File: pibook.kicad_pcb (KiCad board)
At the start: 2 copper layers, 85 x 85 mm, 174 parts, among them IC1 ATTINY48-A, J1 ComputeModule, J2 TRS_JACK_3PIN, P1 CONN_01X40, P2 USB_OTG, P3 CONN_01X02, P4 CONN_02X05, P5 USB_A, P6 CONN_02X06, P7 CONN_01X20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

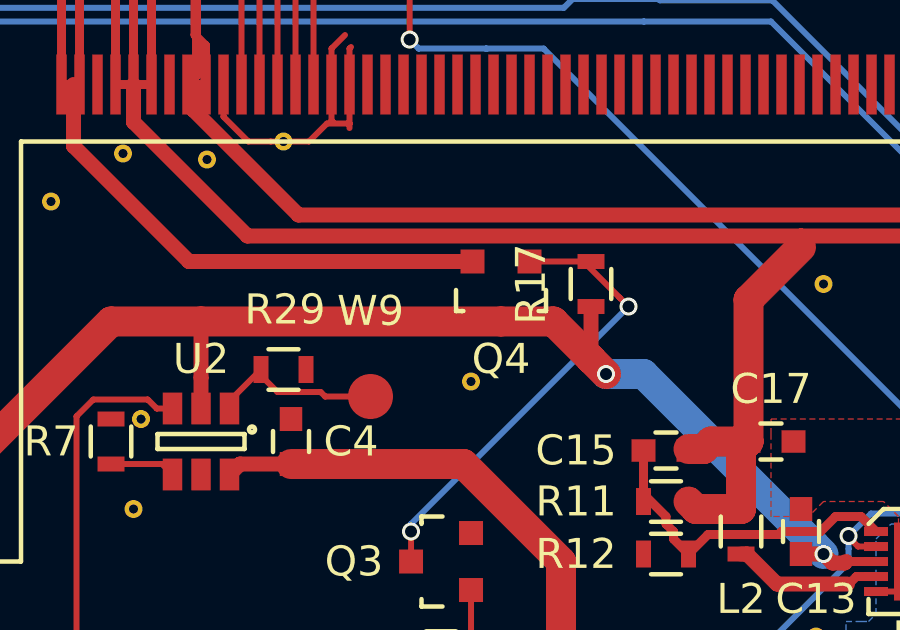
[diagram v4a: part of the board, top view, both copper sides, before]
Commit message: Corrected polarity of mosfet Q4 (switches CM_VBAT)
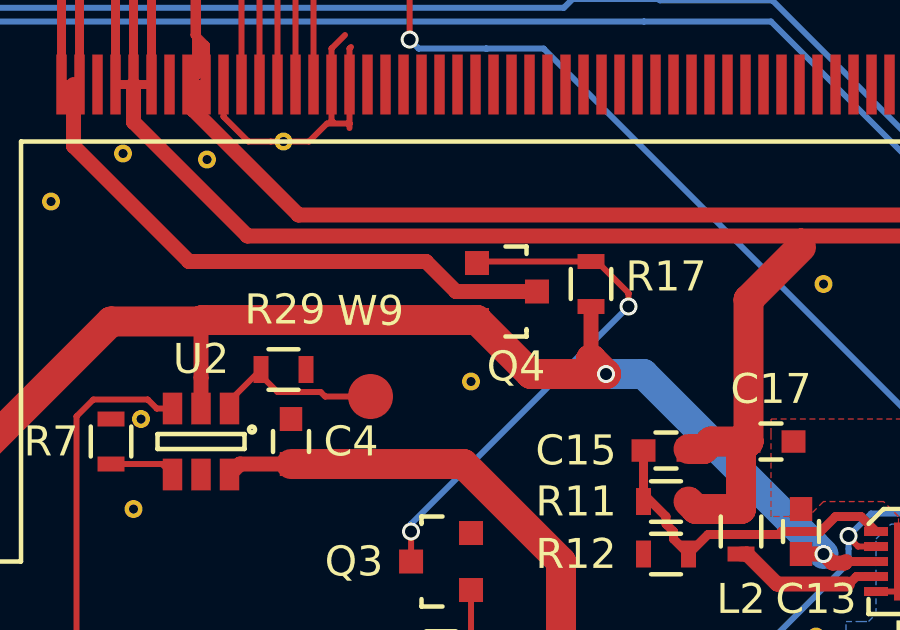
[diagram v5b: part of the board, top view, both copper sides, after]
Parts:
- moved Q4 0.20 mm to (101.2, 176.0), turned to 270 degrees
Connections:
- Q4 pad 2: /CM_VBAT -> +BATT
- Q4 pad 3: +BATT -> /CM_VBAT
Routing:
- net /CM_VBAT: track 38.9 -> 41.5 mm
- net Net-(Q3-Pad3): track 15.4 -> 17.5 mm
- net +BATT: track 300.4 -> 301.2 mm
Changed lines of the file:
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@@
   (general
     (links 404)
-    (no_connects 5)
+    (no_connects 8)
     (area 72.949999 107.949999 158.050001 193.050001)
     (thickness 1.6)
     (drawings 26)
-    (tracks 1700)
+    (tracks 1705)
     (zones 0)
     (modules 174)
@@
   )
   (module TO_SOT_Packages_SMD:SOT-23 (layer F.Cu)
-    (at 101 176 180)
+    (at 101.2 176 270)
     (descr "SOT-23, Standard")
     (tags SOT-23)
     (attr smd)
-    (fp_text reference Q4 (at 0 -2.25 180) (layer F.SilkS)
+    (fp_text reference Q4 (at 2.5 -0.3 360) (layer F.SilkS)
       (effects (font (size 1 1) (thickness 0.15)))
     )
-    (fp_text value Si2323DS (at 0 2.3 180) (layer F.Fab)
+    (fp_text value Si2323DS (at 0 2.3 270) (layer F.Fab)
       (effects (font (size 1 1) (thickness 0.15)))
     )
@@
     (fp_line (start 1.29916 -0.65024) (end 1.49982 -0.65024) (layer F.SilkS) (width 0.15))
     (fp_line (start 1.49982 -0.65024) (end 1.49982 0.0508) (layer F.SilkS) (width 0.15))
-    (pad 1 smd rect (at -0.95 1.00076 180) (size 0.8001 0.8001) (layers F.Cu F.Paste F.Mask)
+    (pad 1 smd rect (at -0.95 1.00076 270) (size 0.8001 0.8001) (layers F.Cu F.Paste F.Mask)
       (net 77 "Net-(Q3-Pad3)"))
-    (pad 2 smd rect (at 0.95 1.00076 180) (size 0.8001 0.8001) (layers F.Cu F.Paste F.Mask)
-      (net 59 /CM_VBAT))
-    (pad 3 smd rect (at 0 -0.99822 180) (size 0.8001 0.8001) (layers F.Cu F.Paste F.Mask)
+    (pad 2 smd rect (at 0.95 1.00076 270) (size 0.8001 0.8001) (layers F.Cu F.Paste F.Mask)
       (net 4 +BATT))
+    (pad 3 smd rect (at 0 -0.99822 270) (size 0.8001 0.8001) (layers F.Cu F.Paste F.Mask)
+      (net 59 /CM_VBAT))
     (model TO_SOT_Packages_SMD.3dshapes/SOT-23.wrl
       (at (xyz 0 0 0))
@@
     (tags "resistor 0603")
     (attr smd)
-    (fp_text reference R17 (at 0 -2 90) (layer F.SilkS)
+    (fp_text reference R17 (at 0.25 2.5 180) (layer F.SilkS)
       (effects (font (size 1 1) (thickness 0.15)))
     )
@@
   (segment (start 137.5997 116) (end 136.5997 117) (width 1) (layer F.Cu) (net 3))
   (segment (start 136.5997 117) (end 134 117) (width 1) (layer F.Cu) (net 3))
+  (segment (start 100.19924 176.95) (end 101.99924 178.75) (width 1) (layer F.Cu) (net 4))
+  (segment (start 101.99924 178.75) (end 104.5 178.75) (width 1) (layer F.Cu) (net 4))
+  (segment (start 91 176.99822) (end 91.04822 176.95) (width 1) (layer F.Cu) (net 4))
+  (segment (start 91.04822 176.95) (end 100.19924 176.95) (width 1) (layer F.Cu) (net 4))
   (segment (start 80.5 187.5) (end 80.5 190) (width 1) (layer F.Cu) (net 4))
   (segment (start 80.5 190) (end 80.5 190.7) (width 1) (layer F.Cu) (net 4))
@@
   (segment (start 104.000008 178.250008) (end 104.5 178.75) (width 1) (layer F.Cu) (net 4))
   (via (at 104.5 178.75) (size 0.6) (drill 0.4) (layers F.Cu B.Cu) (net 4))
-  (segment (start 102.748212 176.99822) (end 104 178.250008) (width 1) (layer F.Cu) (net 4))
-  (segment (start 101 176.99822) (end 102.748212 176.99822) (width 1) (layer F.Cu) (net 4))
   (segment (start 104 176.5) (end 104 178.250008) (width 0.5) (layer F.Cu) (net 4))
   (segment (start 117.25 117.131374) (end 117.25 117.05) (width 0.2) (layer F.Cu) (net 4))
@@
   (segment (start 126.375 128) (end 126.25 128.125) (width 0.5) (layer F.Cu) (net 4))
   (segment (start 88.00178 176.99822) (end 91 176.99822) (width 1) (layer F.Cu) (net 4))
-  (segment (start 91 176.99822) (end 101 176.99822) (width 1) (layer F.Cu) (net 4))
   (segment (start 91 179.9) (end 91 178.87) (width 0.5) (layer F.Cu) (net 4))
   (segment (start 91 178.87) (end 91 176.99822) (width 0.5) (layer F.Cu) (net 4))
@@
   (segment (start 93.25 159.15) (end 93.25 159.7) (width 0.2) (layer F.Cu) (net 58))
   (segment (start 93.25 159.7) (end 93.25 160.9) (width 0.2) (layer F.Cu) (net 58))
+  (segment (start 98.49924 174.99924) (end 99.5 176) (width 0.5) (layer F.Cu) (net 59))
+  (segment (start 99.5 176) (end 102.19822 176) (width 0.5) (layer F.Cu) (net 59))
+  (segment (start 90.59924 174.99924) (end 98.49924 174.99924) (width 0.5) (layer F.Cu) (net 59))
   (segment (start 86.95 165.05) (end 86.95 164.866512) (width 0.3) (layer F.Cu) (net 59))
   (segment (start 86.95 164.866512) (end 87.25 164.566512) (width 0.3) (layer F.Cu) (net 59))
@@
   (segment (start 86.65 164.75) (end 86.95 165.05) (width 0.3) (layer F.Cu) (net 59))
   (segment (start 86.75 169.1) (end 86.75 171.15) (width 0.5) (layer F.Cu) (net 59))
-  (segment (start 90.59924 174.99924) (end 99.14995 174.99924) (width 0.5) (layer F.Cu) (net 59))
   (segment (start 86.75 171.15) (end 90.59924 174.99924) (width 0.5) (layer F.Cu) (net 59))
-  (segment (start 99.14995 174.99924) (end 100.05 174.99924) (width 0.5) (layer F.Cu) (net 59))
   (segment (start 86 158.75) (end 86.65 159.4) (width 0.2) (layer F.Cu) (net 59))
   (segment (start 86.65 159.4) (end 86.65 160.9) (width 0.2) (layer F.Cu) (net 59))
@@
   (segment (start 102.3 190.25) (end 100.05 188) (width 0.2) (layer F.Cu) (net 76))
   (via (at 102.3 190.25) (size 0.6) (drill 0.4) (layers F.Cu B.Cu) (net 76))
+  (segment (start 104 175) (end 100.24924 175) (width 0.2) (layer F.Cu) (net 77))
+  (segment (start 100.24924 175) (end 100.19924 175.05) (width 0.2) (layer F.Cu) (net 77))
+  (segment (start 104 175) (end 104.2 175) (width 0.2) (layer F.Cu) (net 77))
+  (segment (start 104.2 175) (end 105.249994 176.049994) (width 0.2) (layer F.Cu) (net 77))
+  (segment (start 105.249994 176.049994) (end 105.249994 176.075736) (width 0.2) (layer F.Cu) (net 77))
+  (segment (start 105.249994 176.075736) (end 105.249994 176.5) (width 0.2) (layer F.Cu) (net 77))
   (segment (start 98 183.749994) (end 98 183.999962) (width 0.2) (layer B.Cu) (net 77))
   (segment (start 105.249994 176.5) (end 98 183.749994) (width 0.2) (layer B.Cu) (net 77))
@@
   (via (at 98 183.999962) (size 0.6) (drill 0.4) (layers F.Cu B.Cu) (net 77))
   (segment (start 98.00178 184.001742) (end 98 183.999962) (width 0.2) (layer F.Cu) (net 77))
-  (segment (start 103.749234 174.99924) (end 104.949995 176.200001) (width 0.2) (layer F.Cu) (net 77))
-  (segment (start 101.95 174.99924) (end 103.749234 174.99924) (width 0.2) (layer F.Cu) (net 77))
-  (segment (start 104.949995 176.200001) (end 105.249994 176.5) (width 0.2) (layer F.Cu) (net 77))
   (via (at 105.249994 176.5) (size 0.6) (drill 0.4) (layers F.Cu B.Cu) (net 77))
   (segment (start 88 181.75) (end 89.7 181.75) (width 0.2) (layer F.Cu) (net 78))
